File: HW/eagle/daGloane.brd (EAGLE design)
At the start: 100 x 80 mm, 84 parts, among them IC1 MCP1252-33X50, U1 STM32F10XTXU6, X2 USB_MICROB_PLUG_MT

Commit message: changed some values
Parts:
- C4: value 4.7 -> 4.7u
- R14, R19: value 150R -> 270R
- R29: value 330 -> 470R
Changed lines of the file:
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@@
 <?xml version="1.0" encoding="utf-8"?>
 <!DOCTYPE eagle SYSTEM "eagle.dtd">
-<eagle version="6.1">
+<eagle version="6.2">
 <drawing>
 <settings>
@@
 <element name="U$3" library="daGloane" package="MPU6000" value="MPU6000" x="40.5" y="40.5" smashed="yes" rot="R270"/>
 <element name="U$4" library="daGloane" package="SERIAL_QFN4X4-16" value="SERIAL_FT230XQ" x="50.1" y="46.4" smashed="yes"/>
-<element name="R14" library="rcl" package="R0603" value="150R" x="52" y="50.4" smashed="yes">
+<element name="R14" library="rcl" package="R0603" value="270R" x="52" y="50.4" smashed="yes">
 <attribute name="NAME" x="51.51099375" y="51.088996875" size="0.4064" layer="25"/>
 <attribute name="VALUE" x="51.11099375" y="48.368" size="0.4064" layer="27"/>
 </element>
-<element name="R19" library="rcl" package="R0603" value="150R" x="51.5" y="36" smashed="yes" rot="R270">
+<element name="R19" library="rcl" package="R0603" value="270R" x="51.5" y="36" smashed="yes" rot="R270">
 <attribute name="NAME" x="50.48899375" y="36.488990625" size="0.4064" layer="25" rot="R270"/>
 <attribute name="VALUE" x="50.967990625" y="36.388996875" size="0.4064" layer="27" rot="R270"/>
@@
 <attribute name="VALUE" x="46.63" y="32.26" size="0.4064" layer="27"/>
 </element>
-<element name="C4" library="rcl" package="C0603" value="4.7" x="50.3" y="31.5" smashed="yes" rot="R90">
+<element name="C4" library="rcl" package="C0603" value="4.7u" x="50.3" y="31.5" smashed="yes" rot="R90">
 <attribute name="NAME" x="49.73" y="31.23" size="0.4064" layer="25" rot="R90"/>
 <attribute name="VALUE" x="52.84" y="30.23" size="0.4064" layer="27" rot="R90"/>
@@
 <attribute name="VALUE" x="50.395" y="32.77" size="1.27" layer="27" rot="R270"/>
 </element>
-<element name="R29" library="rcl" package="R0603" value="330" x="50.9" y="27.8" smashed="yes" rot="R180">
+<element name="R29" library="rcl" package="R0603" value="470R" x="50.9" y="27.8" smashed="yes" rot="R180">
 <attribute name="NAME" x="50.511" y="28.389" size="0.4064" layer="25"/>
 <attribute name="VALUE" x="51.789" y="29.832" size="0.4064" layer="27" rot="R180"/>

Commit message: resistor values for LEDs changed back; voltage drop over LEDs at 10mA is 2V. Therefore the voltage drop accross the resistor has to be 1.3V (3.3V supply) --> R = 1.3V / 10mA = 130Ohm; next E12 value is 150Ohm.
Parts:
- C4: value 4.7u -> 4.7µF
- R14, R19: value 270R -> 150R
- R29: value 470R -> 330R
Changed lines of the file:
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@@
 <element name="U$3" library="daGloane" package="MPU6000" value="MPU6000" x="40.5" y="40.5" smashed="yes" rot="R270"/>
 <element name="U$4" library="daGloane" package="SERIAL_QFN4X4-16" value="SERIAL_FT230XQ" x="50.1" y="46.4" smashed="yes"/>
-<element name="R14" library="rcl" package="R0603" value="270R" x="52" y="50.4" smashed="yes">
+<element name="R14" library="rcl" package="R0603" value="150R" x="52" y="50.4" smashed="yes">
 <attribute name="NAME" x="51.51099375" y="51.088996875" size="0.4064" layer="25"/>
 <attribute name="VALUE" x="51.11099375" y="48.368" size="0.4064" layer="27"/>
 </element>
-<element name="R19" library="rcl" package="R0603" value="270R" x="51.5" y="36" smashed="yes" rot="R270">
+<element name="R19" library="rcl" package="R0603" value="150R" x="51.5" y="36" smashed="yes" rot="R270">
 <attribute name="NAME" x="50.48899375" y="36.488990625" size="0.4064" layer="25" rot="R270"/>
 <attribute name="VALUE" x="50.967990625" y="36.388996875" size="0.4064" layer="27" rot="R270"/>
@@
 <attribute name="VALUE" x="46.63" y="32.26" size="0.4064" layer="27"/>
 </element>
-<element name="C4" library="rcl" package="C0603" value="4.7u" x="50.3" y="31.5" smashed="yes" rot="R90">
+<element name="C4" library="rcl" package="C0603" value="4.7µF" x="50.3" y="31.5" smashed="yes" rot="R90">
 <attribute name="NAME" x="49.73" y="31.23" size="0.4064" layer="25" rot="R90"/>
 <attribute name="VALUE" x="52.84" y="30.23" size="0.4064" layer="27" rot="R90"/>
@@
 <attribute name="VALUE" x="50.395" y="32.77" size="1.27" layer="27" rot="R270"/>
 </element>
-<element name="R29" library="rcl" package="R0603" value="470R" x="50.9" y="27.8" smashed="yes" rot="R180">
+<element name="R29" library="rcl" package="R0603" value="330R" x="50.9" y="27.8" smashed="yes" rot="R180">
 <attribute name="NAME" x="50.511" y="28.389" size="0.4064" layer="25"/>
 <attribute name="VALUE" x="51.789" y="29.832" size="0.4064" layer="27" rot="R180"/>

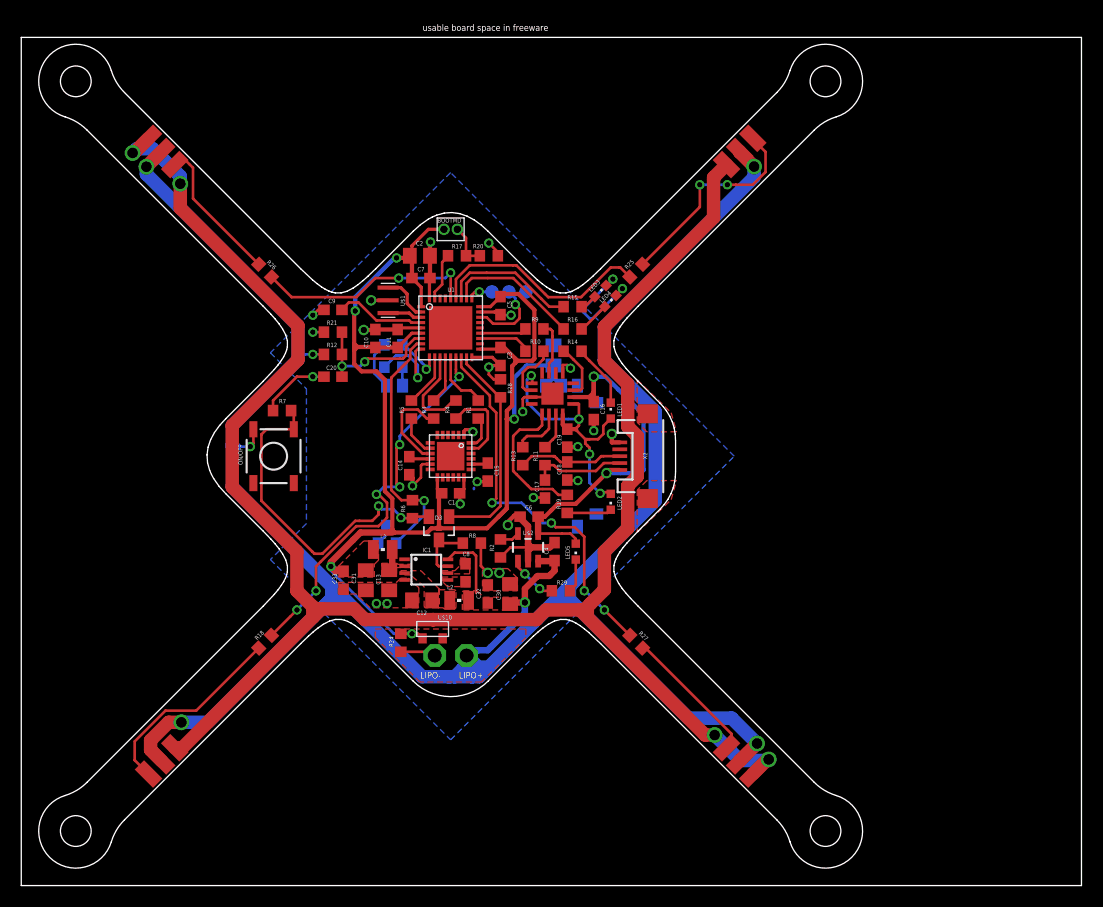
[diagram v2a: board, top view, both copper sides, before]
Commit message: silkscreen of stm32 and FT230 modified outline of maximum usable boadspace in eagle freeware version removed
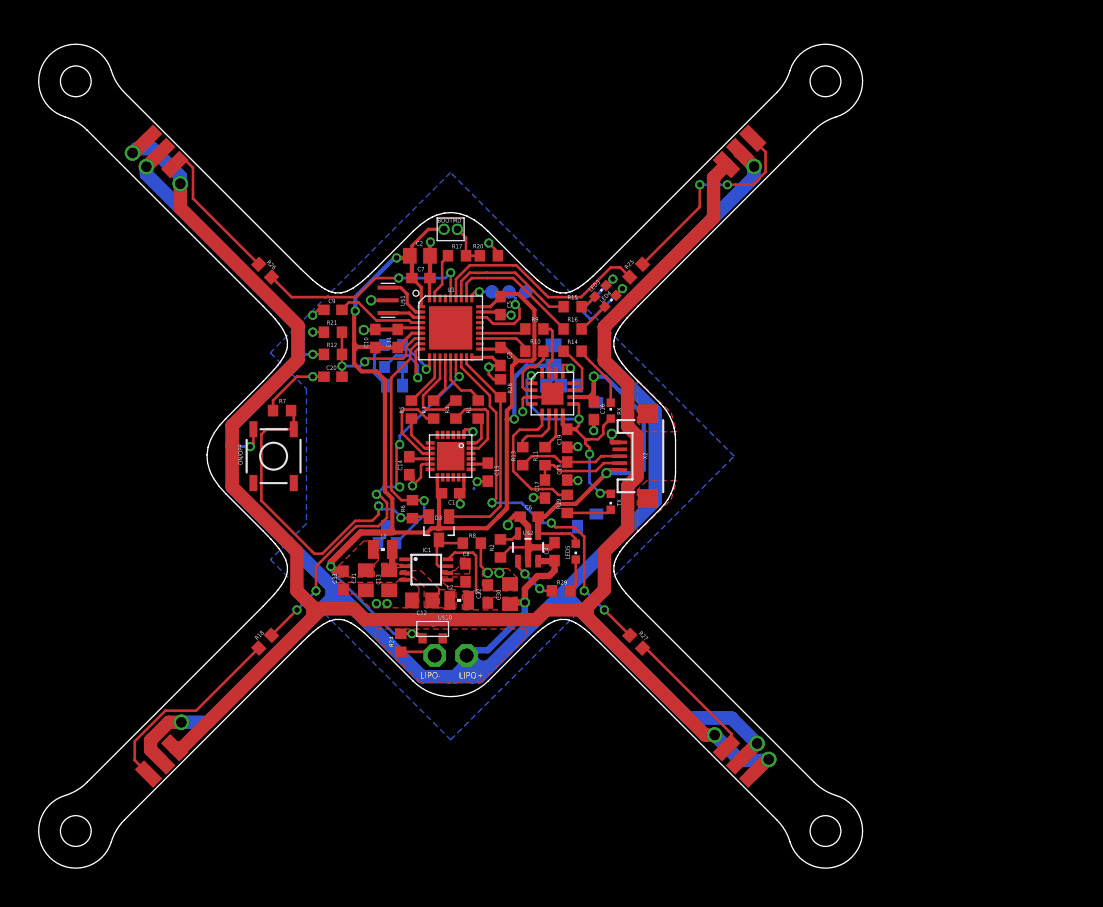
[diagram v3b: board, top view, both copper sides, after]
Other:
- board size 100 x 80 mm -> 77.7 x 77.7 mm
- board text added: "RX"
- board text added: "TX"
- board text removed: "usable board space in freeware"
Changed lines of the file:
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@@
 <board>
 <plain>
-<wire x1="84.99998125" y1="-0.000003125" x2="84.999990625" y2="0.00000625" width="0.01" layer="20"/>
-<wire x1="0" y1="0" x2="0" y2="80" width="0.01" layer="20"/>
-<wire x1="0" y1="80" x2="100" y2="80" width="0.01" layer="20"/>
-<wire x1="100" y1="80" x2="100" y2="0" width="0.01" layer="20"/>
-<wire x1="100" y1="0" x2="0" y2="0" width="0.01" layer="20"/>
-<text x="37.849746875" y="80.6142125" size="0.6096" layer="20" font="vector">usable board space in freeware</text>
 <wire x1="23.87" y1="48.683559375" x2="22.822328125" y2="47.57106875" width="0.01" layer="20"/>
 <wire x1="24.2206625" y1="49.106384375" x2="23.87" y2="48.683559375" width="0.01" layer="20"/>
@@
 <vertex x="32.8" y="33.9"/>
 </polygon>
+<text x="56.6" y="44.4" size="0.4064" layer="25" rot="R90">RX</text>
+<text x="56.6" y="35.8" size="0.4064" layer="25" rot="R90">TX</text>
 </plain>
 <attributes>
@@
 </element>
 <element name="LED1" library="led" package="CHIPLED_0603" value="" x="55.6" y="44.8" smashed="yes">
-<attribute name="NAME" x="56.629996875" y="44.22999375" size="0.4064" layer="25" rot="R90"/>
 <attribute name="VALUE" x="58.14" y="43.52999375" size="1.27" layer="27" rot="R90"/>
 </element>
 <element name="LED2" library="led" package="CHIPLED_0603" value="" x="55.6" y="36.2" smashed="yes" rot="R180">
-<attribute name="NAME" x="56.629996875" y="35.43000625" size="0.4064" layer="25" rot="R90"/>
 <attribute name="VALUE" x="53.06" y="37.46999375" size="1.27" layer="27" rot="R270"/>
 </element>
